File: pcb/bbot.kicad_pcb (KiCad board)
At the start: 2 copper layers, 33 parts, among them P1 CONN_01X03, P2 CONN_01X02, P3 CONN_01X12, U1 BTN8982TA, U2 BTN8982TA, U3 BTN8982TA, U4 AS5045

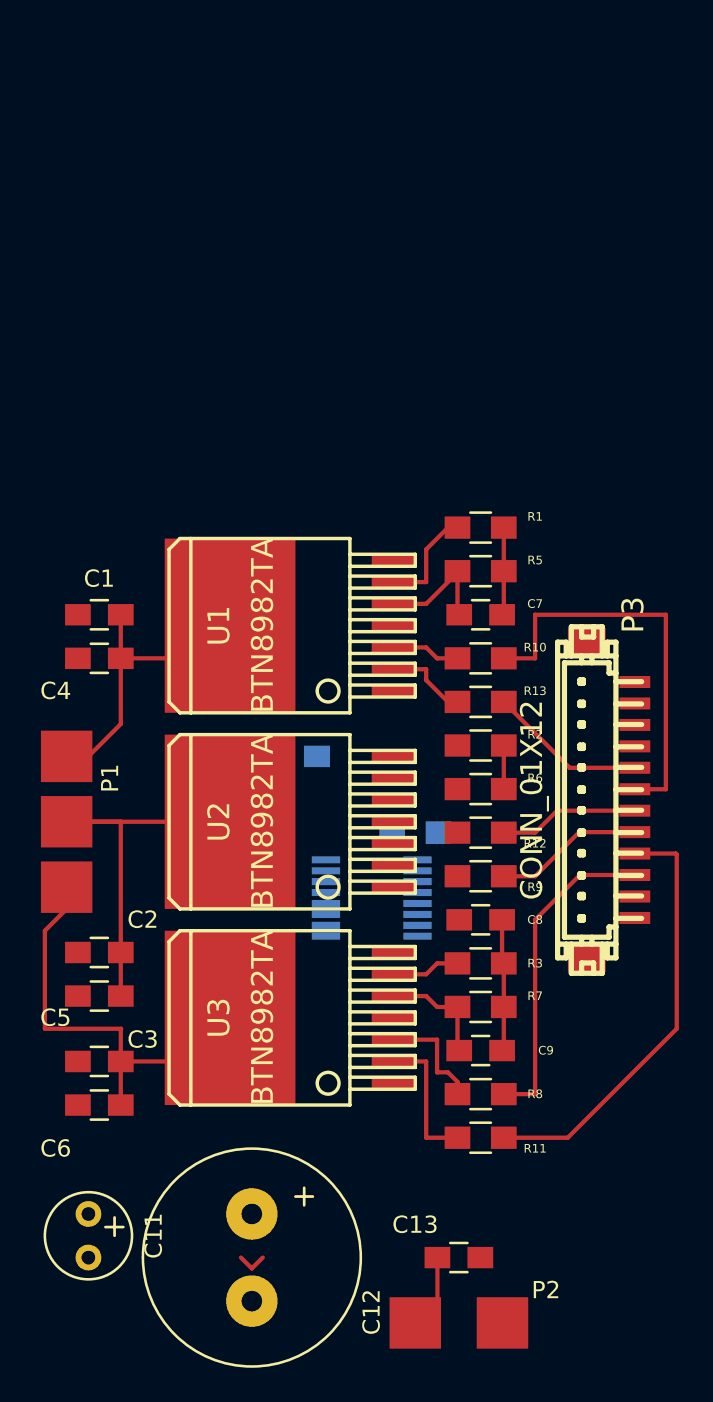
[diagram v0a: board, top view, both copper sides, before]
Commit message: Submitted half bridge v1.0 for fab
Sent to oshpark.
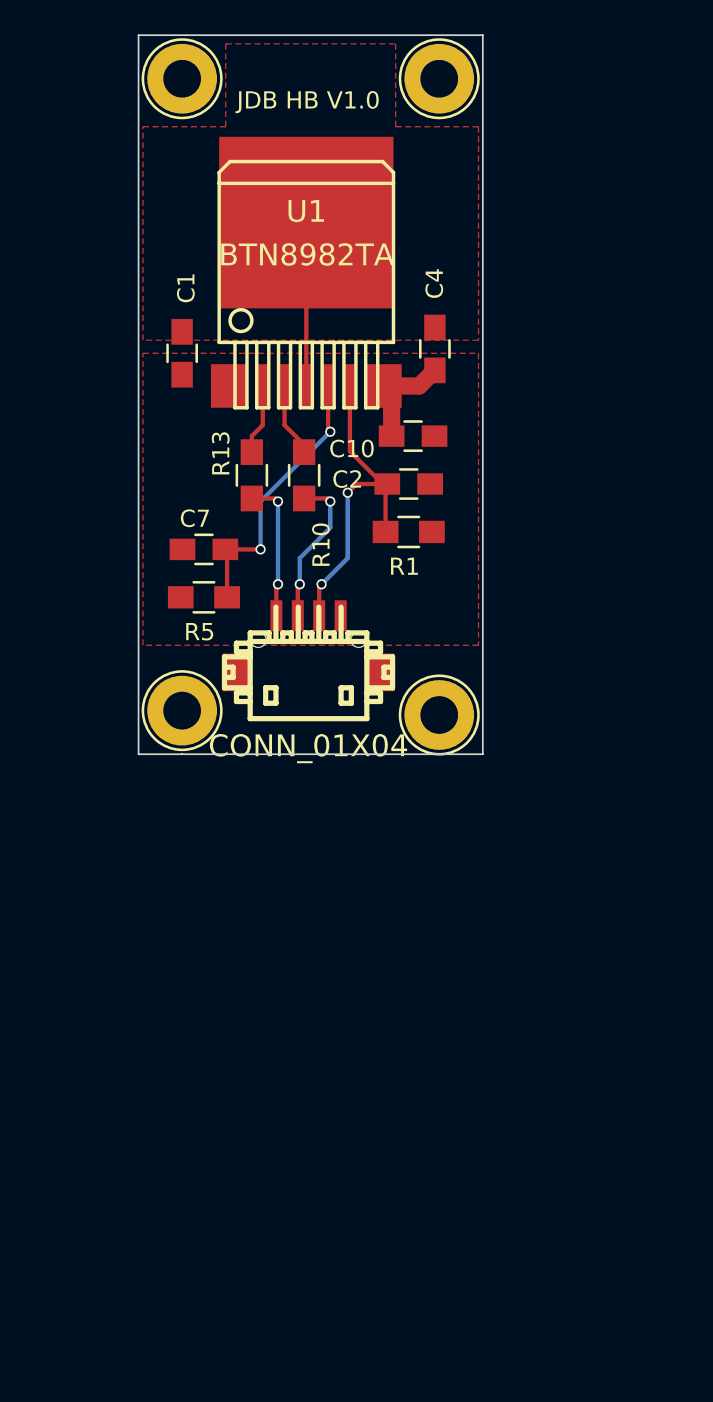
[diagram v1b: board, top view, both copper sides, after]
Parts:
- removed C11: 5uF, Capacitors_Elko_ThroughHole:Elko_vert_11x5mm_RM2.5
- removed C12: 1000uF, Capacitors_Elko_ThroughHole:Elko_vert_25x12.5mm_RM5
- removed C13, C8, C9: 100nF, Capacitors_SMD:C_0805_HandSoldering
- removed C3, C5, C6: 220nF, Capacitors_SMD:C_0805_HandSoldering
- removed P1: CONN_01X03, bbot_footprints:JDB_BLDC_CONN
- removed P2: CONN_01X02, bbot_footprints:JDB_BATT_CONN
- removed R11, R12, R4, R8, R9: 10k, Resistors_SMD:R_0805_HandSoldering
- removed R2, R3: 1k, Resistors_SMD:R_0805_HandSoldering
- removed R6, R7: 0.51k, Resistors_SMD:R_0805_HandSoldering
- removed U2, U3: BTN8982TA, to263:TO263-7
- removed U4: AS5045, ssop16:ssop-16
- added REF**: 1pin, bbot_footprints:1pin, F.Cu at (143.3, 103.4)
- added REF**: 1pin, bbot_footprints:1pin, F.Cu at (158.2, 103.6)
- added REF**: 1pin, bbot_footprints:1pin, F.Cu at (158.2, 66.5)
- added REF**: 1pin, bbot_footprints:1pin, F.Cu at (143.3, 66.5)
- C10: moved to F.Cu
- C2: value 220nF -> 1nF
- P3: value CONN_01X12 -> CONN_01X04; footprint w_conn_df13:df13c-12p-125v -> w_conn_df13:df13-4p-125h
- U1: footprint to263:TO263-7 -> bbot_footprints:BTN8982
- moved C2 32.7 mm to (156.5, 90.2)
- moved C4 26.6 mm to (158.0, 82.3), turned to 90 degrees
- moved C10 19.9 mm to (156.7, 87.4)
- moved R13 18.8 mm to (147.3, 89.7), turned to 90 degrees
- moved P3 18.5 mm to (150.6, 101.3), turned to 0 degrees
- moved C7 16.6 mm to (144.5, 94.0), turned to 180 degrees
- moved R5 16.2 mm to (144.5, 96.8), turned to 180 degrees
- moved C1 16.0 mm to (143.3, 82.5), turned to 90 degrees
- moved U1 14.9 mm to (150.5, 84.5), turned to 0 degrees
- moved R10 14.8 mm to (150.4, 89.7), turned to 90 degrees
- moved R1 4.20 mm to (156.5, 93.0)
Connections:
- net INH_A renamed INH
- net IN_A renamed IN
- net MOTOR_OUT_A renamed MOTOR_OUT
- net SR_A renamed SR
- C10 pad 1: GND -> VCC
- C10 pad 2: +5V -> GND
- C2 pad 1: GND -> IS
- C2 pad 2: MOTOR_OUT_B -> GND
- P3 pad 2: SPI_MISO -> IS
- P3 pad 3: SPI_CLK -> Net-(P3-Pad3)
- P3 pad 4: SPI_CS -> Net-(P3-Pad4)
- R1 pad 1: Net-(R1-Pad1) -> IS
- R10 pad 1: Net-(P3-Pad6) -> Net-(P3-Pad3)
- R13 pad 1: Net-(P3-Pad5) -> Net-(P3-Pad4)
- U1 pad 6: Net-(R1-Pad1) -> IS
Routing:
- net Net-(P3-Pad9): track 25.3 -> 0.00 mm
- net MOTOR_OUT_C: track 25.1 -> 0.00 mm
- net Net-(P3-Pad6): track 24.0 -> 0.00 mm
- net MOTOR_OUT_B: track 21.6 -> 0.00 mm
- net GND: track 20.4 -> 0.00 mm
- net IS: track 0.00 -> 20.0 mm, vias 0 -> 2
- net Net-(P3-Pad10): track 18.9 -> 0.00 mm
- net MOTOR_OUT: track 16.2 -> 4.75 mm
- net Net-(P3-Pad3): track 0.00 -> 9.57 mm, vias 0 -> 2
- net Net-(P3-Pad5): track 9.23 -> 0.00 mm
- net SR: track 7.15 -> 16.3 mm, vias 0 -> 2
- net IN_C: track 8.83 -> 0.00 mm
- net Net-(P3-Pad8): track 8.70 -> 0.00 mm
- net Net-(P3-Pad4): track 0.00 -> 8.30 mm, vias 0 -> 2
- net Net-(P3-Pad7): track 8.17 -> 0.00 mm
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- added copper zone on F.Cu, net GND
- added copper zone on F.Cu, net MOTOR_OUT
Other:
- board outline added: 20.1 x 41.9 mm
- net class Power added: clearance 0.2, trace_width 1, via_dia 0.6, via_drill 0.4
- rule pad_to_mask_clearance: 0.2 -> 0
- board text added: "JDB HB V1.0"
